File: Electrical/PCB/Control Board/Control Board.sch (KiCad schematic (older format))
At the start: 92 parts, among them J1 ED2627-ND, J10 6posheader, J11 S7038-ND, J13 ED1501-ND, J14 ED2989-ND-USB, J15 ED2580-ND, J16 ED2580-ND, J17 ED2744-ND, J18 ED2744-ND, J19 ED2744-ND, J2 ED2627-ND, J20 ED2744-ND, J21 ED2744-ND, J22 ED2744-ND, J23 ED2744-ND, J24 ED2744-ND, J25 ED2744-ND, J26 ED2744-ND, J28 ED2580-ND, J29 ED2580-ND, J3 ED2627-ND, J30 ED2580-ND, J31 ED2580-ND, J4 ED2627-ND, J5 ED2627-ND, J6 S9175-ND, J7 S9175-ND, J8 6posheader, J9 S7038-ND, M1 Mounting_Holes, T1 test_point, T10 test_point, T11 test_point, T12 test_point, T13 test_point, T14 test_point, T15 test_point, T16 test_point, T17 test_point, T18 test_point, T19 test_point, T2 test_point, T20 test_point, T21 test_point, T3 test_point, T4 test_point, T5 test_point, T6 test_point, T7 test_point, T8 test_point, T9 test_point, U1 LM358-N, U2 LM358-N, y1 rover_silkscreen

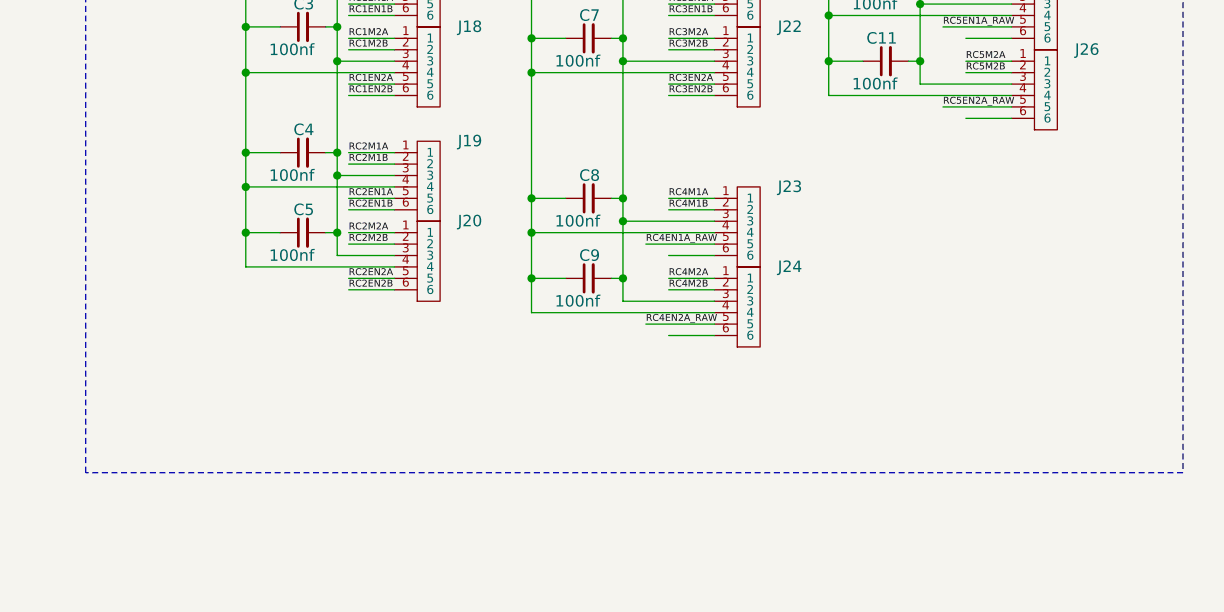
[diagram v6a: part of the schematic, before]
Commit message: Added filter caps for quadrature encoder signals
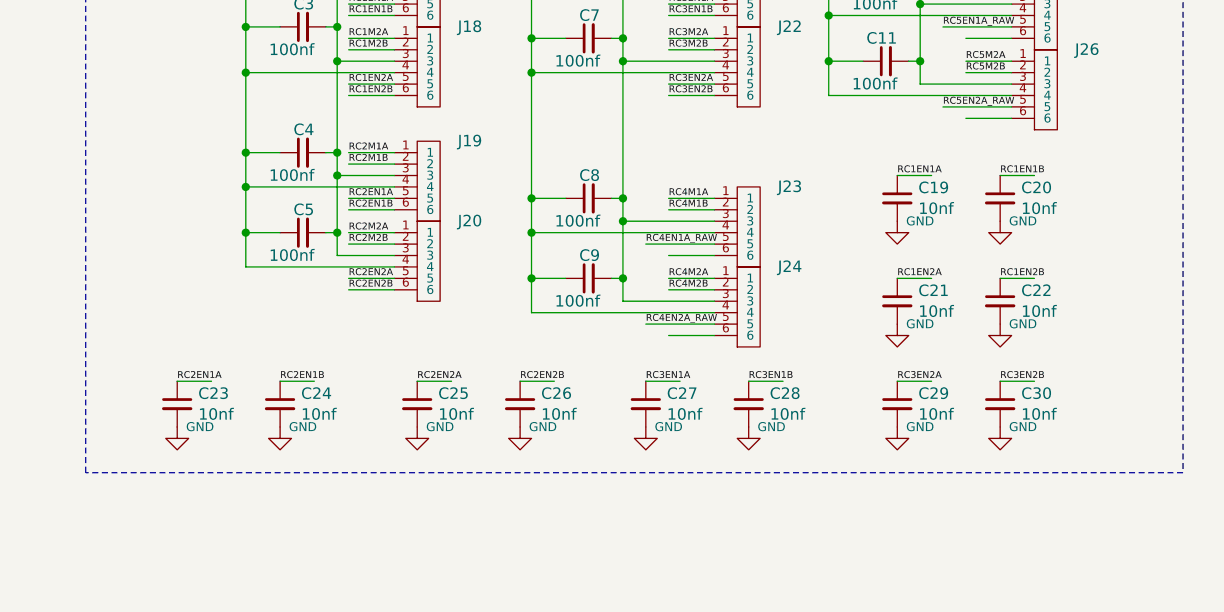
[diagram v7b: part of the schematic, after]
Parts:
- added C19, C20, C21, C22, C23, C24, C25, C26, C27, C28, C29, C30: 10nf, Resistor_THT:R_Axial_DIN0207_L6.3mm_D2.5mm_P7.62mm_Horizontal, symbol Device:C_Small
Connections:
- wire segments 465 -> 477
